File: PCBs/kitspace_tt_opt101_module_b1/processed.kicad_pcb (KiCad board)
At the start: 2 copper layers, 15.2 x 22.9 mm, 4 parts, among them J1 Conn_01x03_Male

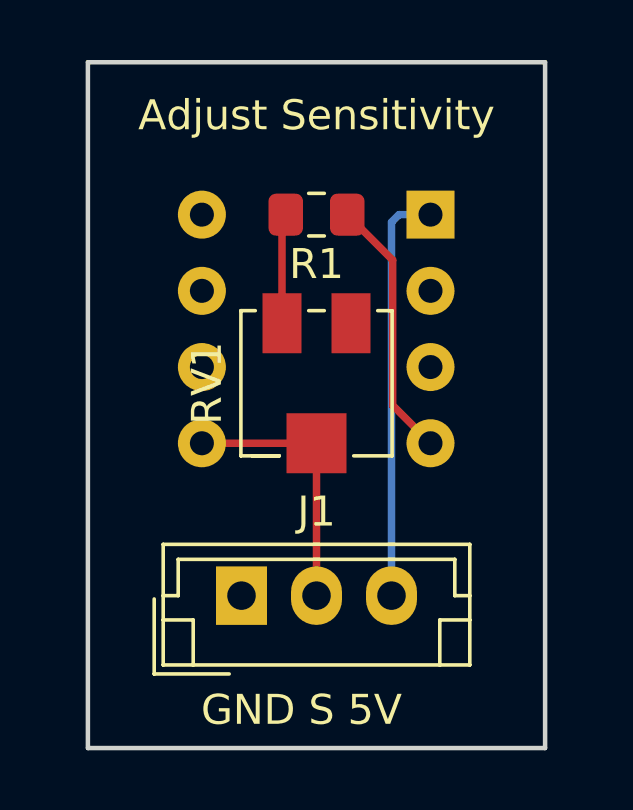
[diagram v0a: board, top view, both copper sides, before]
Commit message: recheck all circuits and clean up fill zone by rerouting the nets using freerouting and manually
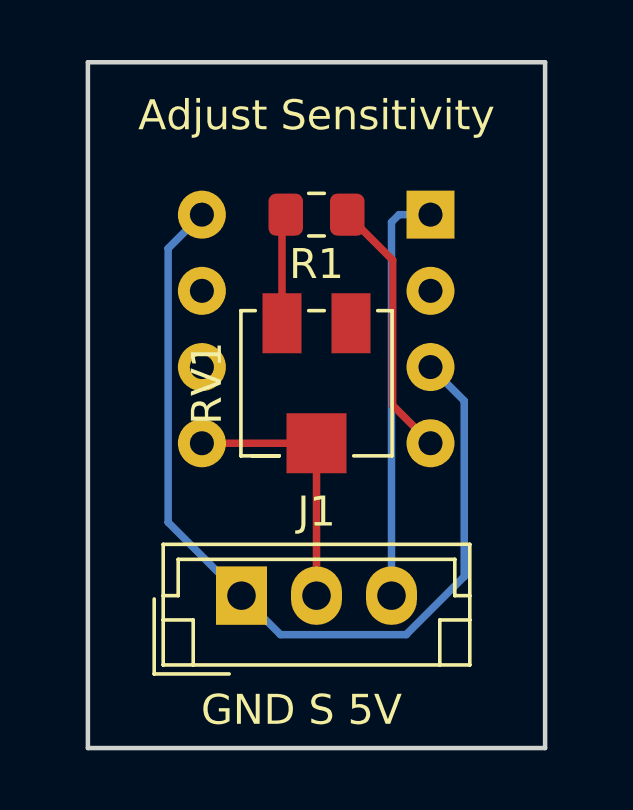
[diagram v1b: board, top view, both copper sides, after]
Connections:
- J1 pad 1: (no net) -> GND
- O1 pad 3: (no net) -> GND
- O1 pad 8: (no net) -> GND
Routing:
- net GND: track 0.00 -> 30.4 mm
